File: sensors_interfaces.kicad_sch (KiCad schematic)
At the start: 25 parts, among them IC601 STK8321, IC602 SP3485EN-L_TR, IC603 WM8782SEDS_RV_C323842, IC604 CS4344-CZZ, IC605 MCP9700AT-E_TT, X601 KF2EDGR-3.81-3P, X602 PJ-327C-4A, X603 PJ-327C-4A

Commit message: changed pin types and fixed 3D-positions
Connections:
- removed net +3.3V: C601.2, C602.2, IC602.8 (VCC), L601.1, R603.2
- removed net GND: C601.1, C602.1, C603.1, C604.1, C605.1, C608.1, C609.1, IC602.5 (GND), IC604.8 (GND), R601.1, R604.1, R605.1, X601.2, X603.1
- new net: C602.2, L601.1
- new net: C601.2, IC602.8 (VCC)
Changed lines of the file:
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@@
     (pin "2")
   )
-  (symbol (lib_id "eduboardv2:CL05B104KB54PNC") (at 166.37 74.93 90) (unit 1)
+  (symbol (lib_name "CL05B104KB54PNC_1") (lib_id "eduboardv2:CL05B104KB54PNC") (at 166.37 74.93 90) (unit 1)
     (in_bom yes) (on_board yes) (fields_autoplaced)
     (property "Reference" "C602" (id 0) (at 170.18 73.6599 90)
@@
     (pin "1")
   )
-  (symbol (lib_id "eduboardv2:GND") (at 203.2 113.03 0) (unit 1)
+  (symbol (lib_name "GND_4") (lib_id "eduboardv2:GND") (at 203.2 113.03 0) (unit 1)
     (in_bom yes) (on_board yes) (fields_autoplaced)
     (property "Reference" "#PWR0612" (id 0) (at 203.2 119.38 0)
@@
     (pin "1")
   )
-  (symbol (lib_id "eduboardv2:GND") (at 86.36 139.7 180) (unit 1)
+  (symbol (lib_name "GND_9") (lib_id "eduboardv2:GND") (at 86.36 139.7 180) (unit 1)
     (in_bom yes) (on_board yes) (fields_autoplaced)
     (property "Reference" "#PWR0604" (id 0) (at 86.36 133.35 0)
@@
     (pin "1")
   )
-  (symbol (lib_id "eduboardv2:0402WGF1002TCE") (at 214.63 85.09 90) (mirror x) (unit 1)
+  (symbol (lib_name "0402WGF1002TCE_3") (lib_id "eduboardv2:0402WGF1002TCE") (at 214.63 85.09 90) (mirror x) (unit 1)
     (in_bom yes) (on_board yes) (fields_autoplaced)
     (property "Reference" "R604" (id 0) (at 217.17 86.3601 90)
@@
     (pin "2")
   )
-  (symbol (lib_id "eduboardv2:PJ-327C-4A") (at 246.38 49.53 0) (mirror y) (unit 1)
+  (symbol (lib_name "PJ-327C-4A_1") (lib_id "eduboardv2:PJ-327C-4A") (at 246.38 49.53 0) (mirror y) (unit 1)
     (in_bom yes) (on_board yes) (fields_autoplaced)
     (property "Reference" "X602" (id 0) (at 256.54 49.5299 0)
@@
     (pin "2")
   )
-  (symbol (lib_id "eduboardv2:GND") (at 241.3 105.41 0) (unit 1)
+  (symbol (lib_name "GND_12") (lib_id "eduboardv2:GND") (at 241.3 105.41 0) (unit 1)
     (in_bom yes) (on_board yes) (fields_autoplaced)
     (property "Reference" "#PWR0617" (id 0) (at 241.3 111.76 0)
@@
     (pin "2")
   )
-  (symbol (lib_id "eduboardv2:GND") (at 214.63 80.01 180) (unit 1)
+  (symbol (lib_name "GND_13") (lib_id "eduboardv2:GND") (at 214.63 80.01 180) (unit 1)
     (in_bom yes) (on_board yes) (fields_autoplaced)
     (property "Reference" "#PWR0613" (id 0) (at 214.63 73.66 0)
@@
     (pin "3")
   )
-  (symbol (lib_id "eduboardv2:GND") (at 166.37 78.74 0) (unit 1)
+  (symbol (lib_name "GND_3") (lib_id "eduboardv2:GND") (at 166.37 78.74 0) (unit 1)
     (in_bom yes) (on_board yes)
     (property "Reference" "#PWR0608" (id 0) (at 166.37 85.09 0)
@@
     (pin "1")
   )
-  (symbol (lib_id "eduboardv2:GND") (at 67.31 168.91 0) (unit 1)
+  (symbol (lib_name "GND_10") (lib_id "eduboardv2:GND") (at 67.31 168.91 0) (unit 1)
     (in_bom yes) (on_board yes) (fields_autoplaced)
     (property "Reference" "#PWR0602" (id 0) (at 67.31 175.26 0)
@@
     (pin "1")
   )
-  (symbol (lib_id "eduboardv2:0402WGF4700TCE") (at 222.25 90.17 0) (mirror y) (unit 1)
+  (symbol (lib_name "0402WGF4700TCE_1") (lib_id "eduboardv2:0402WGF4700TCE") (at 222.25 90.17 0) (mirror y) (unit 1)
     (in_bom yes) (on_board yes)
     (property "Reference" "R606" (id 0) (at 222.25 92.71 0))
@@
     (pin "2")
   )
-  (symbol (lib_id "eduboardv2:GND") (at 107.95 158.75 270) (unit 1)
+  (symbol (lib_name "GND_8") (lib_id "eduboardv2:GND") (at 107.95 158.75 270) (unit 1)
     (in_bom yes) (on_board yes)
     (property "Reference" "#PWR0606" (id 0) (at 101.6 158.75 0)
@@
     (pin "1")
   )
-  (symbol (lib_id "eduboardv2:CL10A106MA8NRNC") (at 166.37 109.22 90) (unit 1)
+  (symbol (lib_name "CL10A106MA8NRNC_1") (lib_id "eduboardv2:CL10A106MA8NRNC") (at 166.37 109.22 90) (unit 1)
     (in_bom yes) (on_board yes) (fields_autoplaced)
     (property "Reference" "C603" (id 0) (at 170.18 107.9499 90)
@@
     (pin "2")
   )
-  (symbol (lib_id "eduboardv2:0402WGF1002TCE") (at 86.36 171.45 90) (mirror x) (unit 1)
+  (symbol (lib_name "0402WGF1002TCE_2") (lib_id "eduboardv2:0402WGF1002TCE") (at 86.36 171.45 90) (mirror x) (unit 1)
     (in_bom yes) (on_board yes) (fields_autoplaced)
     (property "Reference" "R603" (id 0) (at 88.9 172.7201 90)
@@
     (pin "3")
   )
-  (symbol (lib_id "eduboardv2:CL10A475KO8NNNC") (at 205.74 97.79 0) (unit 1)
+  (symbol (lib_name "CL10A475KO8NNNC_1") (lib_id "eduboardv2:CL10A475KO8NNNC") (at 205.74 97.79 0) (unit 1)
     (in_bom yes) (on_board yes)
     (property "Reference" "C607" (id 0) (at 208.28 99.06 0))
@@
     (pin "4")
   )
-  (symbol (lib_id "eduboardv2:CL05B104KB54PNC") (at 189.23 74.93 90) (unit 1)
+  (symbol (lib_name "CL05B104KB54PNC_2") (lib_id "eduboardv2:CL05B104KB54PNC") (at 189.23 74.93 90) (unit 1)
     (in_bom yes) (on_board yes) (fields_autoplaced)
     (property "Reference" "C604" (id 0) (at 193.04 73.6599 90)
@@
     (pin "2")
   )
-  (symbol (lib_id "eduboardv2:GND") (at 196.85 95.25 90) (unit 1)
+  (symbol (lib_name "GND_2") (lib_id "eduboardv2:GND") (at 196.85 95.25 90) (unit 1)
     (in_bom yes) (on_board yes) (fields_autoplaced)
     (property "Reference" "#PWR0611" (id 0) (at 203.2 95.25 0)
@@
     (pin "1")
   )
-  (symbol (lib_id "eduboardv2:GND") (at 229.87 82.55 180) (unit 1)
+  (symbol (lib_name "GND_11") (lib_id "eduboardv2:GND") (at 229.87 82.55 180) (unit 1)
     (in_bom yes) (on_board yes) (fields_autoplaced)
     (property "Reference" "#PWR0615" (id 0) (at 229.87 76.2 0)
@@
     (pin "1")
   )
-  (symbol (lib_id "eduboardv2:GND") (at 189.23 78.74 0) (unit 1)
+  (symbol (lib_name "GND_6") (lib_id "eduboardv2:GND") (at 189.23 78.74 0) (unit 1)
     (in_bom yes) (on_board yes)
     (property "Reference" "#PWR0610" (id 0) (at 189.23 85.09 0)
@@
     (pin "1")
   )
-  (symbol (lib_id "eduboardv2:GND") (at 166.37 113.03 0) (unit 1)
+  (symbol (lib_name "GND_1") (lib_id "eduboardv2:GND") (at 166.37 113.03 0) (unit 1)
     (in_bom yes) (on_board yes) (fields_autoplaced)
     (property "Reference" "#PWR0609" (id 0) (at 166.37 119.38 0)
@@
     (pin "1")
   )
-  (symbol (lib_id "eduboardv2:0402B222K500NT") (at 229.87 86.36 90) (mirror x) (unit 1)
+  (symbol (lib_name "0402B222K500NT_1") (lib_id "eduboardv2:0402B222K500NT") (at 229.87 86.36 90) (mirror x) (unit 1)
     (in_bom yes) (on_board yes) (fields_autoplaced)
     (property "Reference" "C608" (id 0) (at 233.68 87.6301 90)
@@
     (pin "2")
   )
-  (symbol (lib_id "eduboardv2:GND") (at 214.63 107.95 0) (unit 1)
+  (symbol (lib_name "GND_5") (lib_id "eduboardv2:GND") (at 214.63 107.95 0) (unit 1)
     (in_bom yes) (on_board yes) (fields_autoplaced)
     (property "Reference" "#PWR0614" (id 0) (at 214.63 114.3 0)
@@
     (pin "1")
   )
-  (symbol (lib_id "eduboardv2:+3.3V") (at 86.36 176.53 180) (unit 1)
+  (symbol (lib_name "+3.3V_2") (lib_id "eduboardv2:+3.3V") (at 86.36 176.53 180) (unit 1)
     (in_bom yes) (on_board yes) (fields_autoplaced)
     (property "Reference" "#PWR0605" (id 0) (at 86.36 172.72 0)
@@
     (pin "2")
   )
-  (symbol (lib_id "eduboardv2:+3.3V") (at 157.48 71.12 0) (unit 1)
+  (symbol (lib_name "+3.3V_1") (lib_id "eduboardv2:+3.3V") (at 157.48 71.12 0) (unit 1)
     (in_bom yes) (on_board yes) (fields_autoplaced)
     (property "Reference" "#PWR0607" (id 0) (at 157.48 74.93 0)
@@
     (pin "1")
   )
-  (symbol (lib_id "eduboardv2:0402WGF1002TCE") (at 86.36 144.78 90) (mirror x) (unit 1)
+  (symbol (lib_name "0402WGF1002TCE_1") (lib_id "eduboardv2:0402WGF1002TCE") (at 86.36 144.78 90) (mirror x) (unit 1)
     (in_bom yes) (on_board yes) (fields_autoplaced)
     (property "Reference" "R601" (id 0) (at 88.9 146.0501 90)
@@
     (pin "9")
   )
-  (symbol (lib_id "eduboardv2:GND") (at 72.39 147.32 0) (unit 1)
+  (symbol (lib_name "GND_7") (lib_id "eduboardv2:GND") (at 72.39 147.32 0) (unit 1)
     (in_bom yes) (on_board yes) (fields_autoplaced)
     (property "Reference" "#PWR0603" (id 0) (at 72.39 153.67 0)

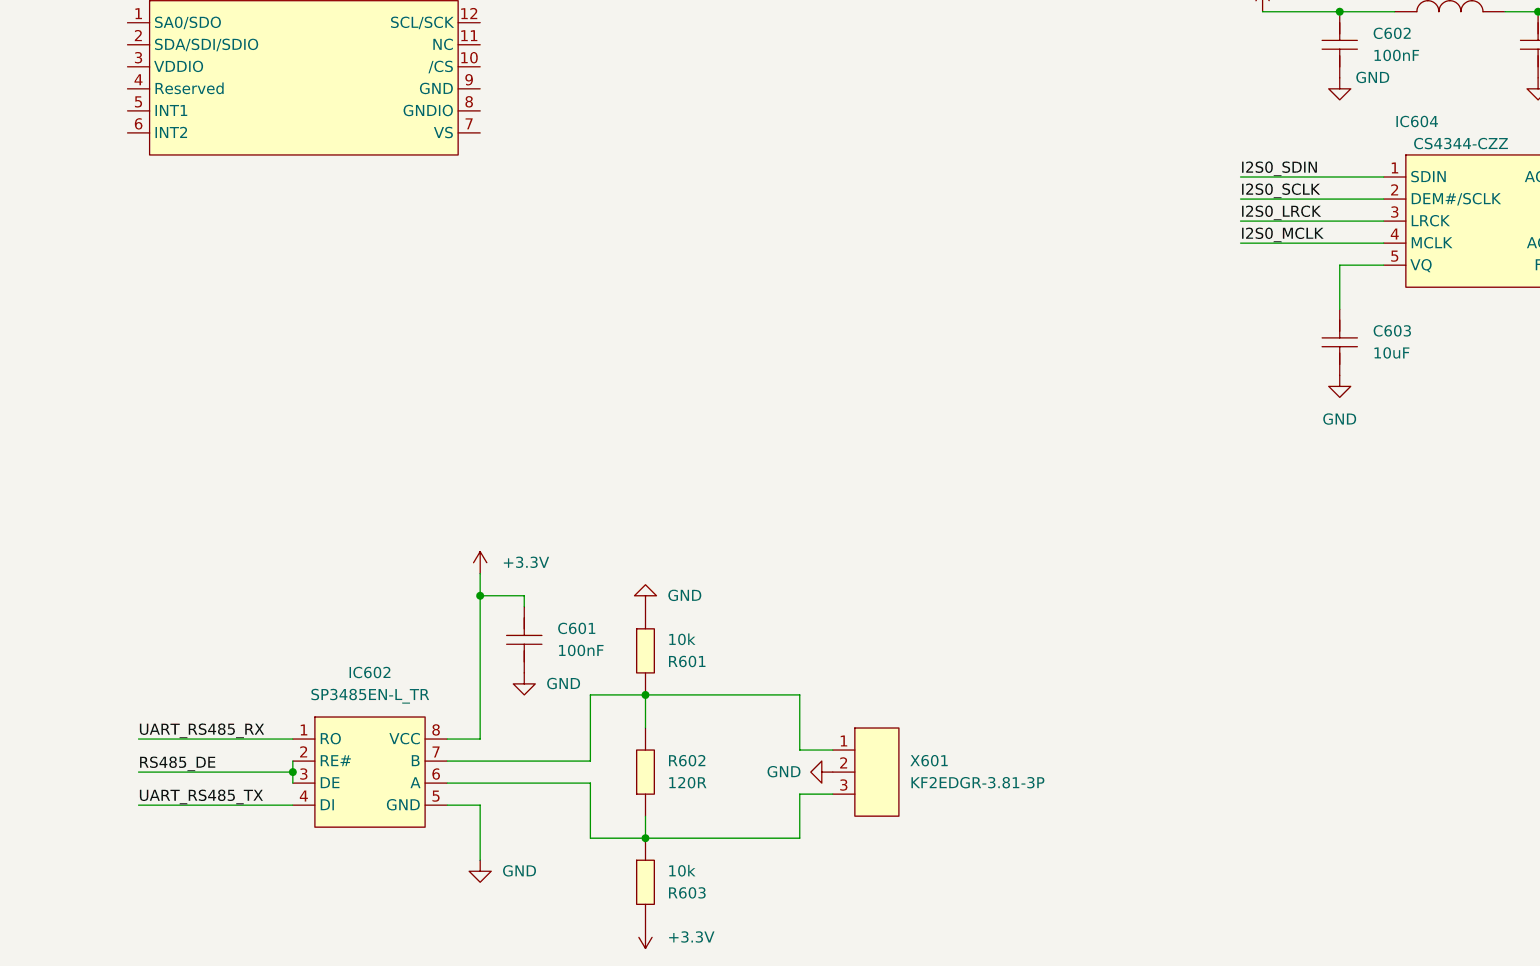
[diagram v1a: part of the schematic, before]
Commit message: change all local labels to global labels.
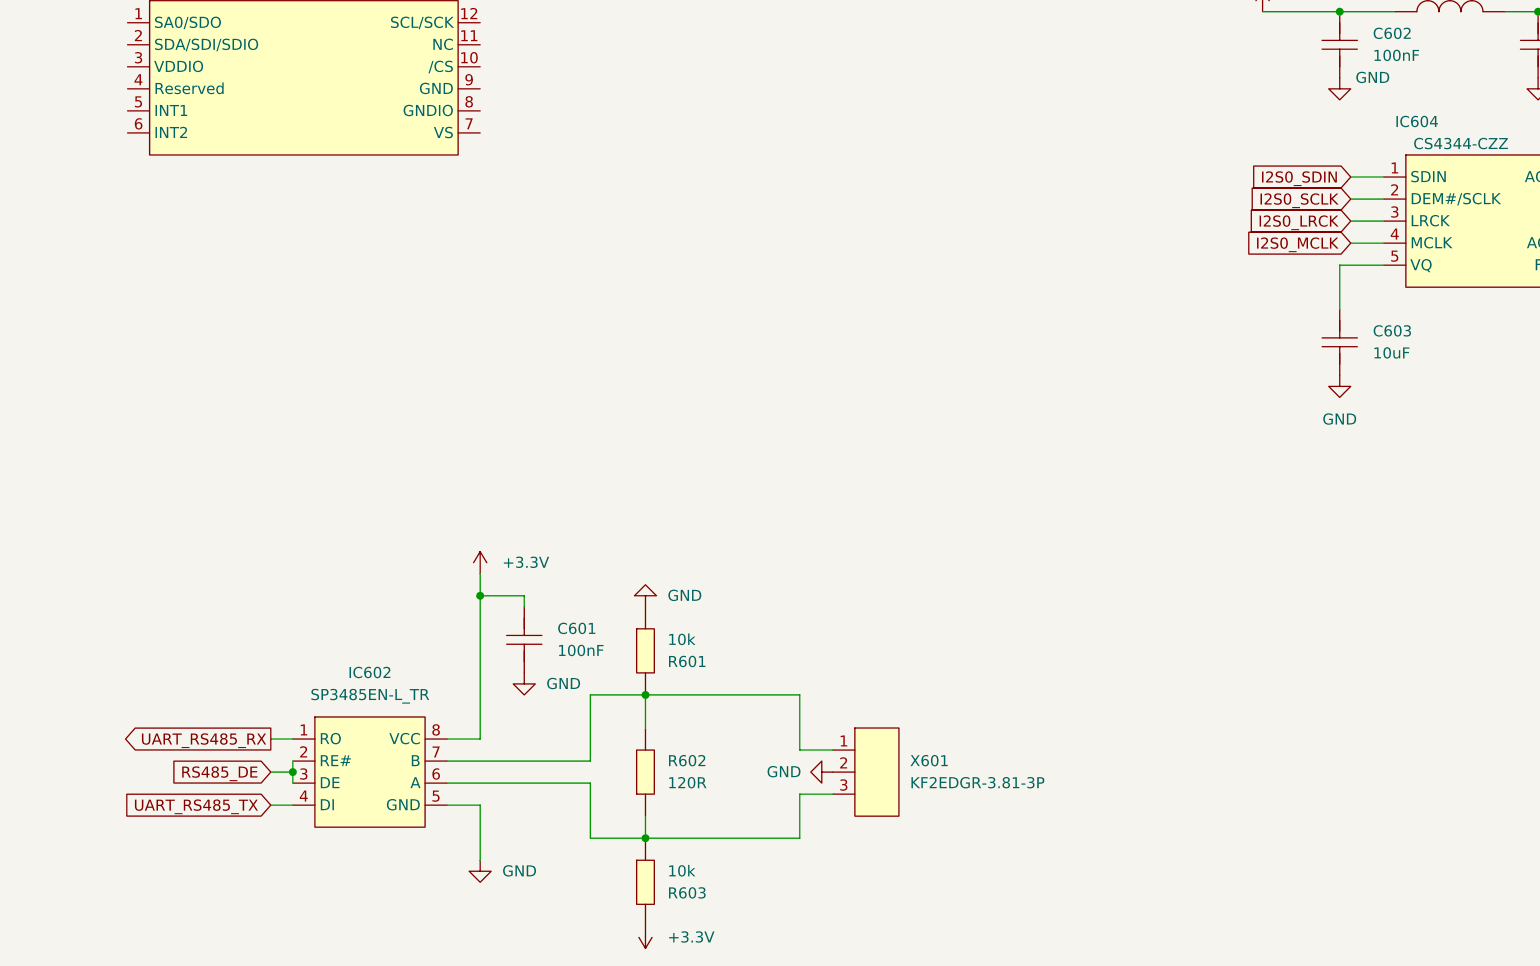
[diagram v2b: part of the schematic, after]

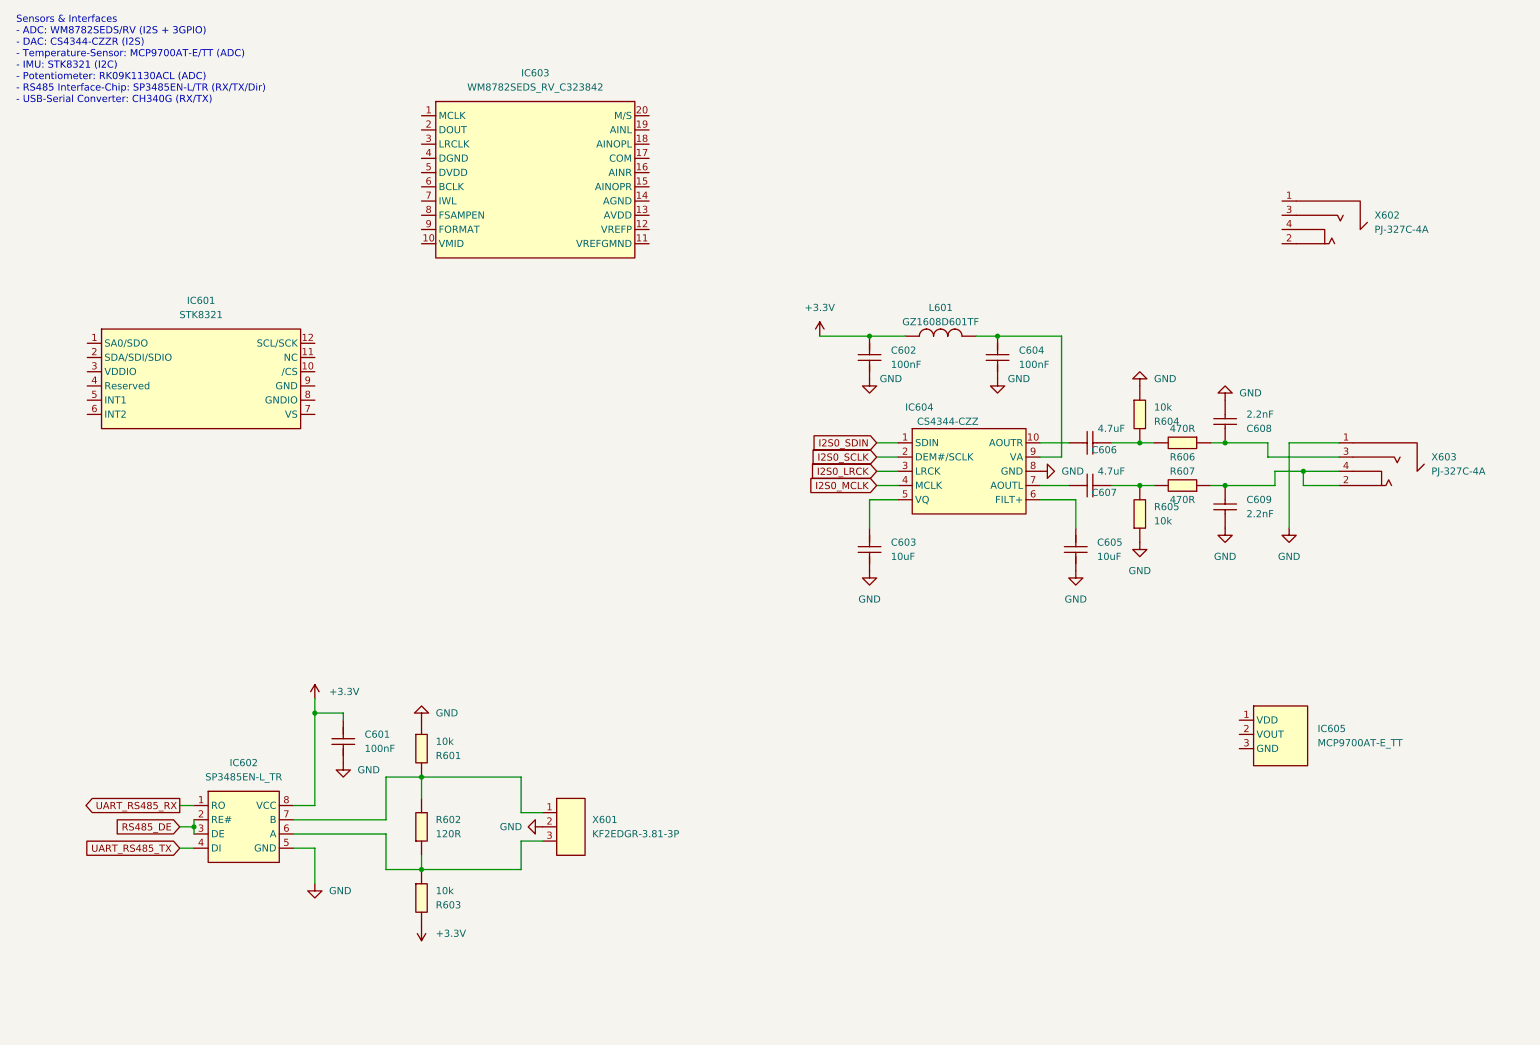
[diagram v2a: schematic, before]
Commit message: move USB Serial Converter and USB Connector to correct pages
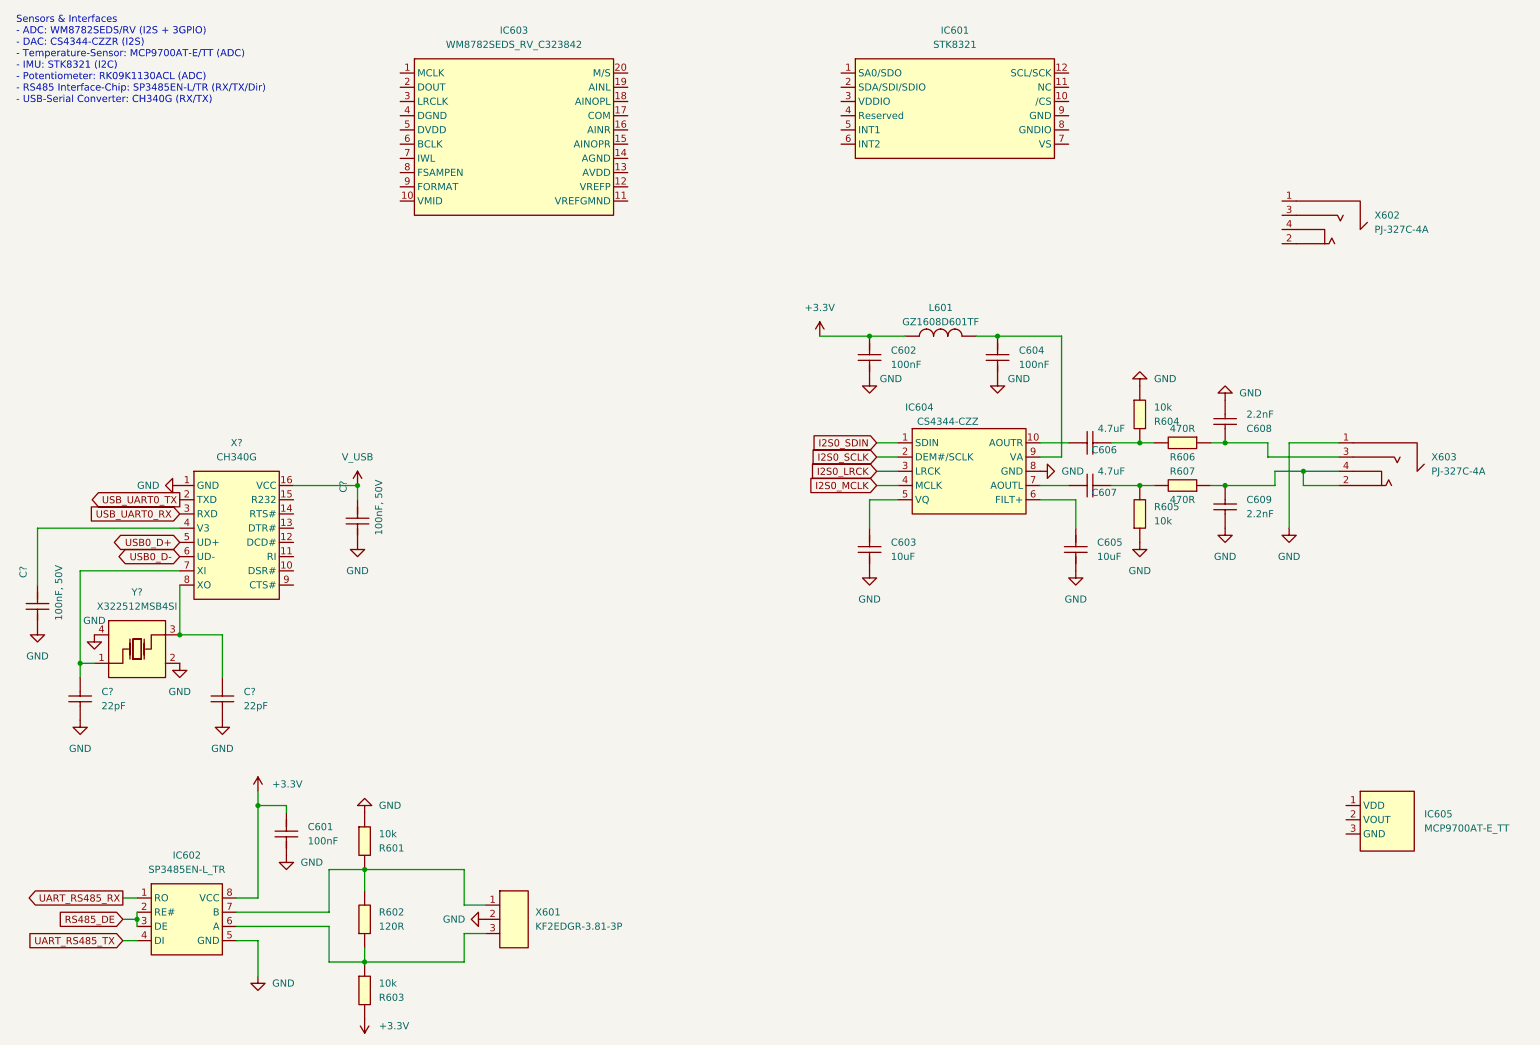
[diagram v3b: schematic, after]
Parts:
- added C? (x2): 100nF, 50V, C0402, symbol eduboardv2:CL05B104KB54PNC
- added C? (x2): 22pF, C0402, symbol eduboardv2:0402CG220J500NT
- added X?: CH340G, SOIC-16_L9.9-W3.9-P1.27-LS6.0-BL, symbol eduboardv2:CH340G
- added Y?: X322512MSB4SI, OSC-SMD_4P-L3.2-W2.5-BL, symbol eduboardv2:X322512MSB4SI
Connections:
- new net: C?.2, X?.4 (V3)
- new net: C?.2, X?.8 (XO), Y?.3 (OSC2)
- new net: C?.2, X?.16 (VCC)
- new net: C?.2, X?.7 (XI), Y?.1 (OSC1)
- new net USB0_D+: X?.5 (UD+)
- new net USB0_D-: X?.6 (UD-)
- new net USB_UART0_RX: X?.3 (RXD)
- new net USB_UART0_TX: X?.2 (TXD)
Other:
- moved on the sheet: C601, IC601, IC602, IC603, IC605, R601, R602, R603, X601
